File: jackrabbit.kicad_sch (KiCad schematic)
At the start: 62 parts, among them J1 USB_C, J2 PinHeader_2.54mm_02x10, J3 PinHeader_2.54mm_02x04, J4 PinHeader_2.54mm_02x04, J5 PinHeader_2.54mm_01x04, J6 PinHeader_2.54mm_01x03, SW1 SW_Push, SW2 SW_Push, U1 MIC5319-3.3YD5, U2 74LVX245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

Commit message: Continue layout
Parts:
- J2: footprint Connector_PinHeader_2.54mm:PinHeader_2x10_P2.54mm_Horizontal -> jackrabbit:PinHeader_2x10_P2.54mm_Horizontal_NoSilk
- J5: footprint Connector_PinHeader_2.54mm:PinHeader_1x04_P2.54mm_Vertical -> jackrabbit:PinHeader_1x04_P2.54mm_NoSilk
- J6: footprint Connector_PinHeader_2.54mm:PinHeader_1x03_P2.54mm_Vertical -> jackrabbit:PinHeader_1x03_P2.54mm_NoSilk
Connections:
- net ADC0: now also J3.7 (Pin_7)
- net D+: now reaches R4.1, U4.47 (USB_DP)
- net D-: now reaches R5.1, U4.46 (USB_DM)
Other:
- moved on the sheet: R4, R5
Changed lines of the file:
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@@
     (stroke (width 0) (type default) (color 0 0 0 0))
   )
+  (wire (pts (xy 166.37 73.66) (xy 173.99 73.66))
+    (stroke (width 0) (type default) (color 0 0 0 0))
+  )
   (wire (pts (xy 246.38 114.3) (xy 236.22 114.3))
     (stroke (width 0) (type default) (color 0 0 0 0))
@@
     (stroke (width 0) (type default) (color 0 0 0 0))
   )
-  (wire (pts (xy 166.37 73.66) (xy 171.45 73.66))
-    (stroke (width 0) (type default) (color 0 0 0 0))
-  )
   (wire (pts (xy 246.38 68.58) (xy 236.22 68.58))
     (stroke (width 0) (type default) (color 0 0 0 0))
@@
     (stroke (width 0) (type default) (color 0 0 0 0))
   )
-  (wire (pts (xy 176.53 71.12) (xy 186.69 71.12))
+  (wire (pts (xy 179.07 71.12) (xy 189.23 71.12))
     (stroke (width 0) (type default) (color 0 0 0 0))
   )
@@
     (stroke (width 0) (type default) (color 0 0 0 0))
   )
-  (wire (pts (xy 166.37 71.12) (xy 171.45 71.12))
+  (wire (pts (xy 166.37 71.12) (xy 173.99 71.12))
     (stroke (width 0) (type default) (color 0 0 0 0))
   )
@@
     (stroke (width 0) (type default) (color 0 0 0 0))
   )
-  (wire (pts (xy 176.53 73.66) (xy 186.69 73.66))
+  (wire (pts (xy 179.07 73.66) (xy 189.23 73.66))
     (stroke (width 0) (type default) (color 0 0 0 0))
   )
@@
     (effects (font (size 1.27 1.27)) (justify left bottom))
   )
-  (label "USB_D+" (at 186.69 71.12 180)
+  (label "USB_D+" (at 189.23 71.12 180)
     (effects (font (size 1.27 1.27)) (justify right bottom))
   )
@@
     (effects (font (size 1.27 1.27)) (justify right bottom))
   )
+  (label "D-" (at 167.64 73.66 0)
+    (effects (font (size 1.27 1.27)) (justify left bottom))
+  )
+  (label "D+" (at 167.64 71.12 0)
+    (effects (font (size 1.27 1.27)) (justify left bottom))
+  )
   (label "OUT_DIG7" (at 53.34 152.4 180)
     (effects (font (size 1.27 1.27)) (justify right bottom))
@@
     (effects (font (size 1.27 1.27)) (justify right bottom))
   )
-  (label "ADC0" (at 233.68 139.7 0)
+  (label "ADC0" (at 233.68 142.24 0)
     (effects (font (size 1.27 1.27)) (justify left bottom))
   )
@@
     (effects (font (size 1.27 1.27)) (justify left bottom))
   )
-  (label "USB_D-" (at 186.69 73.66 180)
+  (label "USB_D-" (at 189.23 73.66 180)
     (effects (font (size 1.27 1.27)) (justify right bottom))
   )
@@
     (pin "1")
   )
-  (symbol (lib_id "Device:R_Small_US") (at 173.99 71.12 90) (unit 1)
+  (symbol (lib_id "Device:R_Small_US") (at 176.53 71.12 90) (unit 1)
     (in_bom yes) (on_board yes)
-    (property "Reference" "R4" (id 0) (at 170.18 69.85 90))
-    (property "Value" "27" (id 1) (at 176.53 69.85 90))
-    (property "Footprint" "Resistor_SMD:R_0603_1608Metric_Pad0.98x0.95mm_HandSolder" (id 2) (at 173.99 71.12 0)
+    (property "Reference" "R4" (id 0) (at 172.72 69.85 90))
+    (property "Value" "27" (id 1) (at 179.07 69.85 90))
+    (property "Footprint" "Resistor_SMD:R_0603_1608Metric_Pad0.98x0.95mm_HandSolder" (id 2) (at 176.53 71.12 0)
       (effects (font (size 1.27 1.27)) hide)
     )
-    (property "Datasheet" "~" (id 3) (at 173.99 71.12 0)
+    (property "Datasheet" "~" (id 3) (at 176.53 71.12 0)
       (effects (font (size 1.27 1.27)) hide)
     )
@@
     (property "Reference" "J2" (id 0) (at 36.83 139.7 0))
     (property "Value" "PinHeader_2.54mm_02x10" (id 1) (at 36.83 167.64 0))
-    (property "Footprint" "Connector_PinHeader_2.54mm:PinHeader_2x10_P2.54mm_Horizontal" (id 2) (at 35.56 154.94 0)
+    (property "Footprint" "jackrabbit:PinHeader_2x10_P2.54mm_Horizontal_NoSilk" (id 2) (at 35.56 154.94 0)
       (effects (font (size 1.27 1.27)) hide)
     )
@@
     (pin "1")
   )
-  (symbol (lib_id "Device:R_Small_US") (at 173.99 73.66 90) (unit 1)
+  (symbol (lib_id "Device:R_Small_US") (at 176.53 73.66 90) (unit 1)
     (in_bom yes) (on_board yes)
-    (property "Reference" "R5" (id 0) (at 170.18 72.39 90))
-    (property "Value" "27" (id 1) (at 176.53 72.39 90))
-    (property "Footprint" "Resistor_SMD:R_0603_1608Metric_Pad0.98x0.95mm_HandSolder" (id 2) (at 173.99 73.66 0)
+    (property "Reference" "R5" (id 0) (at 172.72 72.39 90))
+    (property "Value" "27" (id 1) (at 179.07 72.39 90))
+    (property "Footprint" "Resistor_SMD:R_0603_1608Metric_Pad0.98x0.95mm_HandSolder" (id 2) (at 176.53 73.66 0)
       (effects (font (size 1.27 1.27)) hide)
     )
-    (property "Datasheet" "~" (id 3) (at 173.99 73.66 0)
+    (property "Datasheet" "~" (id 3) (at 176.53 73.66 0)
       (effects (font (size 1.27 1.27)) hide)
     )
@@
     (property "Reference" "J6" (id 0) (at 30.48 186.69 0))
     (property "Value" "PinHeader_2.54mm_01x03" (id 1) (at 30.48 196.85 0))
-    (property "Footprint" "Connector_PinHeader_2.54mm:PinHeader_1x03_P2.54mm_Vertical" (id 2) (at 30.48 191.77 0)
+    (property "Footprint" "jackrabbit:PinHeader_1x03_P2.54mm_NoSilk" (id 2) (at 30.48 191.77 0)
       (effects (font (size 1.27 1.27)) hide)
     )
@@
     (property "Reference" "J5" (id 0) (at 200.66 152.4 0))
     (property "Value" "PinHeader_2.54mm_01x04" (id 1) (at 200.66 165.1 0))
-    (property "Footprint" "Connector_PinHeader_2.54mm:PinHeader_1x04_P2.54mm_Vertical" (id 2) (at 200.66 157.48 0)
+    (property "Footprint" "jackrabbit:PinHeader_1x04_P2.54mm_NoSilk" (id 2) (at 200.66 157.48 0)
       (effects (font (size 1.27 1.27)) hide)
     )
@@
     )
     (path "/791214ba-3f08-4a8f-b2f1-03e7cde5a47c"
-      (reference "J2") (unit 1) (value "PinHeader_2.54mm_02x10") (footprint "Connector_PinHeader_2.54mm:PinHeader_2x10_P2.54mm_Horizontal")
+      (reference "J2") (unit 1) (value "PinHeader_2.54mm_02x10") (footprint "jackrabbit:PinHeader_2x10_P2.54mm_Horizontal_NoSilk")
     )
     (path "/41267881-d459-44ec-a16d-7e8810cd8184"
@@
     )
     (path "/c422dfdf-189d-45aa-8572-20905ff07ea7"
-      (reference "J5") (unit 1) (value "PinHeader_2.54mm_01x04") (footprint "Connector_PinHeader_2.54mm:PinHeader_1x04_P2.54mm_Vertical")
+      (reference "J5") (unit 1) (value "PinHeader_2.54mm_01x04") (footprint "jackrabbit:PinHeader_1x04_P2.54mm_NoSilk")
     )
     (path "/bbb69503-a53a-4fa5-9940-c051d2dd833e"
-      (reference "J6") (unit 1) (value "PinHeader_2.54mm_01x03") (footprint "Connector_PinHeader_2.54mm:PinHeader_1x03_P2.54mm_Vertical")
+      (reference "J6") (unit 1) (value "PinHeader_2.54mm_01x03") (footprint "jackrabbit:PinHeader_1x03_P2.54mm_NoSilk")
     )
     (path "/92912fe5-8afd-4b87-83be-55234c82a217"

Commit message: Continue layout
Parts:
- J3, J4: footprint Connector_PinHeader_2.54mm:PinHeader_2x04_P2.54mm_Horizontal -> jackrabbit:PinHeader_2x04_P2.54mm_NoSilk
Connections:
- net ~{DIR_OUT_B}: now also U4.29 (GPIO18); no longer U4.28 (GPIO17)
- net ~{OE_A}: now also U4.28 (GPIO17); no longer U4.31 (GPIO20)
- net ~{OE_B}: now also U4.30 (GPIO19); no longer U4.32 (GPIO21)
- net at R7.1: now also U4.31 (GPIO20); no longer U4.29 (GPIO18)
- net at R8.1: now also U4.32 (GPIO21); no longer U4.30 (GPIO19)
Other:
- moved on the sheet: R7, R8
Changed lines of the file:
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@@
     (stroke (width 0) (type default) (color 0 0 0 0))
   )
-  (wire (pts (xy 176.53 127) (xy 187.96 127))
+  (wire (pts (xy 176.53 132.08) (xy 187.96 132.08))
     (stroke (width 0) (type default) (color 0 0 0 0))
   )
@@
     (stroke (width 0) (type default) (color 0 0 0 0))
   )
-  (wire (pts (xy 176.53 129.54) (xy 187.96 129.54))
+  (wire (pts (xy 176.53 134.62) (xy 187.96 134.62))
     (stroke (width 0) (type default) (color 0 0 0 0))
   )
@@
     (stroke (width 0) (type default) (color 0 0 0 0))
   )
-  (wire (pts (xy 166.37 132.08) (xy 177.8 132.08))
+  (wire (pts (xy 166.37 124.46) (xy 177.8 124.46))
     (stroke (width 0) (type default) (color 0 0 0 0))
   )
@@
     (stroke (width 0) (type default) (color 0 0 0 0))
   )
-  (wire (pts (xy 166.37 134.62) (xy 177.8 134.62))
+  (wire (pts (xy 166.37 129.54) (xy 177.8 129.54))
     (stroke (width 0) (type default) (color 0 0 0 0))
   )
@@
     (stroke (width 0) (type default) (color 0 0 0 0))
   )
-  (wire (pts (xy 166.37 129.54) (xy 171.45 129.54))
+  (wire (pts (xy 166.37 134.62) (xy 171.45 134.62))
     (stroke (width 0) (type default) (color 0 0 0 0))
   )
@@
     (stroke (width 0) (type default) (color 0 0 0 0))
   )
-  (wire (pts (xy 166.37 124.46) (xy 177.8 124.46))
+  (wire (pts (xy 166.37 127) (xy 177.8 127))
     (stroke (width 0) (type default) (color 0 0 0 0))
   )
@@
     (stroke (width 0) (type default) (color 0 0 0 0))
   )
-  (wire (pts (xy 166.37 127) (xy 171.45 127))
+  (wire (pts (xy 166.37 132.08) (xy 171.45 132.08))
     (stroke (width 0) (type default) (color 0 0 0 0))
   )
@@
     (effects (font (size 1.27 1.27)) (justify right bottom))
   )
-  (label "RX" (at 187.96 129.54 180)
+  (label "RX" (at 187.96 134.62 180)
     (effects (font (size 1.27 1.27)) (justify right bottom))
   )
@@
     (effects (font (size 1.27 1.27)) (justify left bottom))
   )
-  (label "~{OE_B}" (at 177.8 134.62 180)
+  (label "~{OE_B}" (at 177.8 129.54 180)
     (effects (font (size 1.27 1.27)) (justify right bottom))
   )
@@
     (effects (font (size 1.27 1.27)) (justify left bottom))
   )
-  (label "TX" (at 187.96 127 180)
+  (label "TX" (at 187.96 132.08 180)
     (effects (font (size 1.27 1.27)) (justify right bottom))
   )
@@
     (effects (font (size 1.27 1.27)) (justify right bottom))
   )
-  (label "~{DIR_OUT_B}" (at 177.8 124.46 180)
+  (label "~{DIR_OUT_B}" (at 177.8 127 180)
     (effects (font (size 1.27 1.27)) (justify right bottom))
   )
@@
     (effects (font (size 1.27 1.27)) (justify left bottom))
   )
-  (label "~{OE_A}" (at 177.8 132.08 180)
+  (label "~{OE_A}" (at 177.8 124.46 180)
     (effects (font (size 1.27 1.27)) (justify right bottom))
   )
@@
     (property "Reference" "J3" (id 0) (at 250.19 139.7 0))
     (property "Value" "PinHeader_2.54mm_02x04" (id 1) (at 250.19 152.4 0))
-    (property "Footprint" "Connector_PinHeader_2.54mm:PinHeader_2x04_P2.54mm_Horizontal" (id 2) (at 248.92 147.32 0)
+    (property "Footprint" "jackrabbit:PinHeader_2x04_P2.54mm_NoSilk" (id 2) (at 248.92 147.32 0)
       (effects (font (size 1.27 1.27)) hide)
     )
@@
     (property "Reference" "J4" (id 0) (at 250.19 154.94 0))
     (property "Value" "PinHeader_2.54mm_02x04" (id 1) (at 250.19 167.64 0))
-    (property "Footprint" "Connector_PinHeader_2.54mm:PinHeader_2x04_P2.54mm_Horizontal" (id 2) (at 248.92 160.02 0)
+    (property "Footprint" "jackrabbit:PinHeader_2x04_P2.54mm_NoSilk" (id 2) (at 248.92 160.02 0)
       (effects (font (size 1.27 1.27)) hide)
     )
@@
     (pin "1")
   )
-  (symbol (lib_id "Device:R_Small_US") (at 173.99 129.54 90) (unit 1)
+  (symbol (lib_id "Device:R_Small_US") (at 173.99 134.62 90) (unit 1)
     (in_bom yes) (on_board yes)
-    (property "Reference" "R8" (id 0) (at 170.18 128.27 90))
-    (property "Value" "100" (id 1) (at 177.8 128.27 90))
-    (property "Footprint" "Resistor_SMD:R_0603_1608Metric_Pad0.98x0.95mm_HandSolder" (id 2) (at 173.99 129.54 0)
+    (property "Reference" "R8" (id 0) (at 170.18 133.35 90))
+    (property "Value" "100" (id 1) (at 177.8 133.35 90))
+    (property "Footprint" "Resistor_SMD:R_0603_1608Metric_Pad0.98x0.95mm_HandSolder" (id 2) (at 173.99 134.62 0)
       (effects (font (size 1.27 1.27)) hide)
     )
-    (property "Datasheet" "~" (id 3) (at 173.99 129.54 0)
+    (property "Datasheet" "~" (id 3) (at 173.99 134.62 0)
       (effects (font (size 1.27 1.27)) hide)
     )
@@
     (pin "2")
   )
-  (symbol (lib_id "Device:R_Small_US") (at 173.99 127 90) (unit 1)
+  (symbol (lib_id "Device:R_Small_US") (at 173.99 132.08 90) (unit 1)
     (in_bom yes) (on_board yes)
-    (property "Reference" "R7" (id 0) (at 170.18 125.73 90))
-    (property "Value" "100" (id 1) (at 177.8 125.73 90))
-    (property "Footprint" "Resistor_SMD:R_0603_1608Metric_Pad0.98x0.95mm_HandSolder" (id 2) (at 173.99 127 0)
+    (property "Reference" "R7" (id 0) (at 170.18 130.81 90))
+    (property "Value" "100" (id 1) (at 177.8 130.81 90))
+    (property "Footprint" "Resistor_SMD:R_0603_1608Metric_Pad0.98x0.95mm_HandSolder" (id 2) (at 173.99 132.08 0)
       (effects (font (size 1.27 1.27)) hide)
     )
-    (property "Datasheet" "~" (id 3) (at 173.99 127 0)
+    (property "Datasheet" "~" (id 3) (at 173.99 132.08 0)
       (effects (font (size 1.27 1.27)) hide)
     )
@@
     )
     (path "/41267881-d459-44ec-a16d-7e8810cd8184"
-      (reference "J3") (unit 1) (value "PinHeader_2.54mm_02x04") (footprint "Connector_PinHeader_2.54mm:PinHeader_2x04_P2.54mm_Horizontal")
+      (reference "J3") (unit 1) (value "PinHeader_2.54mm_02x04") (footprint "jackrabbit:PinHeader_2x04_P2.54mm_NoSilk")
     )
     (path "/42c076d8-84e3-453f-aa5b-cae6866038f5"
-      (reference "J4") (unit 1) (value "PinHeader_2.54mm_02x04") (footprint "Connector_PinHeader_2.54mm:PinHeader_2x04_P2.54mm_Horizontal")
+      (reference "J4") (unit 1) (value "PinHeader_2.54mm_02x04") (footprint "jackrabbit:PinHeader_2x04_P2.54mm_NoSilk")
     )
     (path "/c422dfdf-189d-45aa-8572-20905ff07ea7"

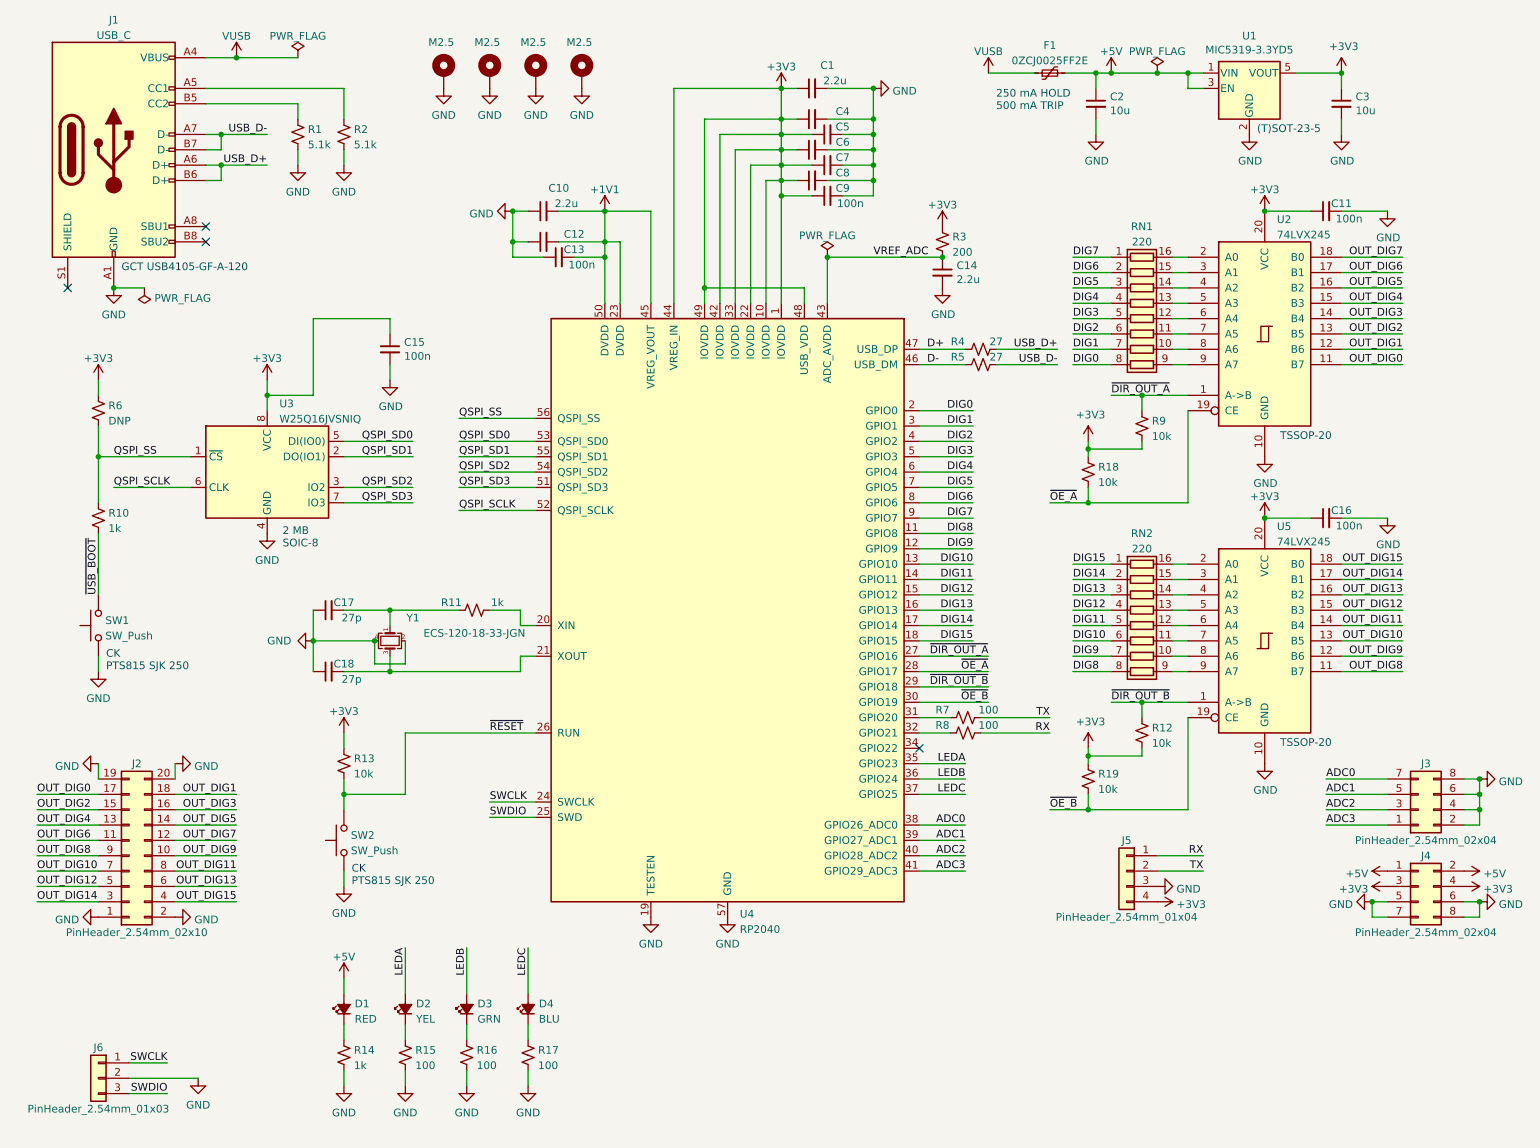
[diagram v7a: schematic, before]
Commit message: Continue layout; add labels for digital connector
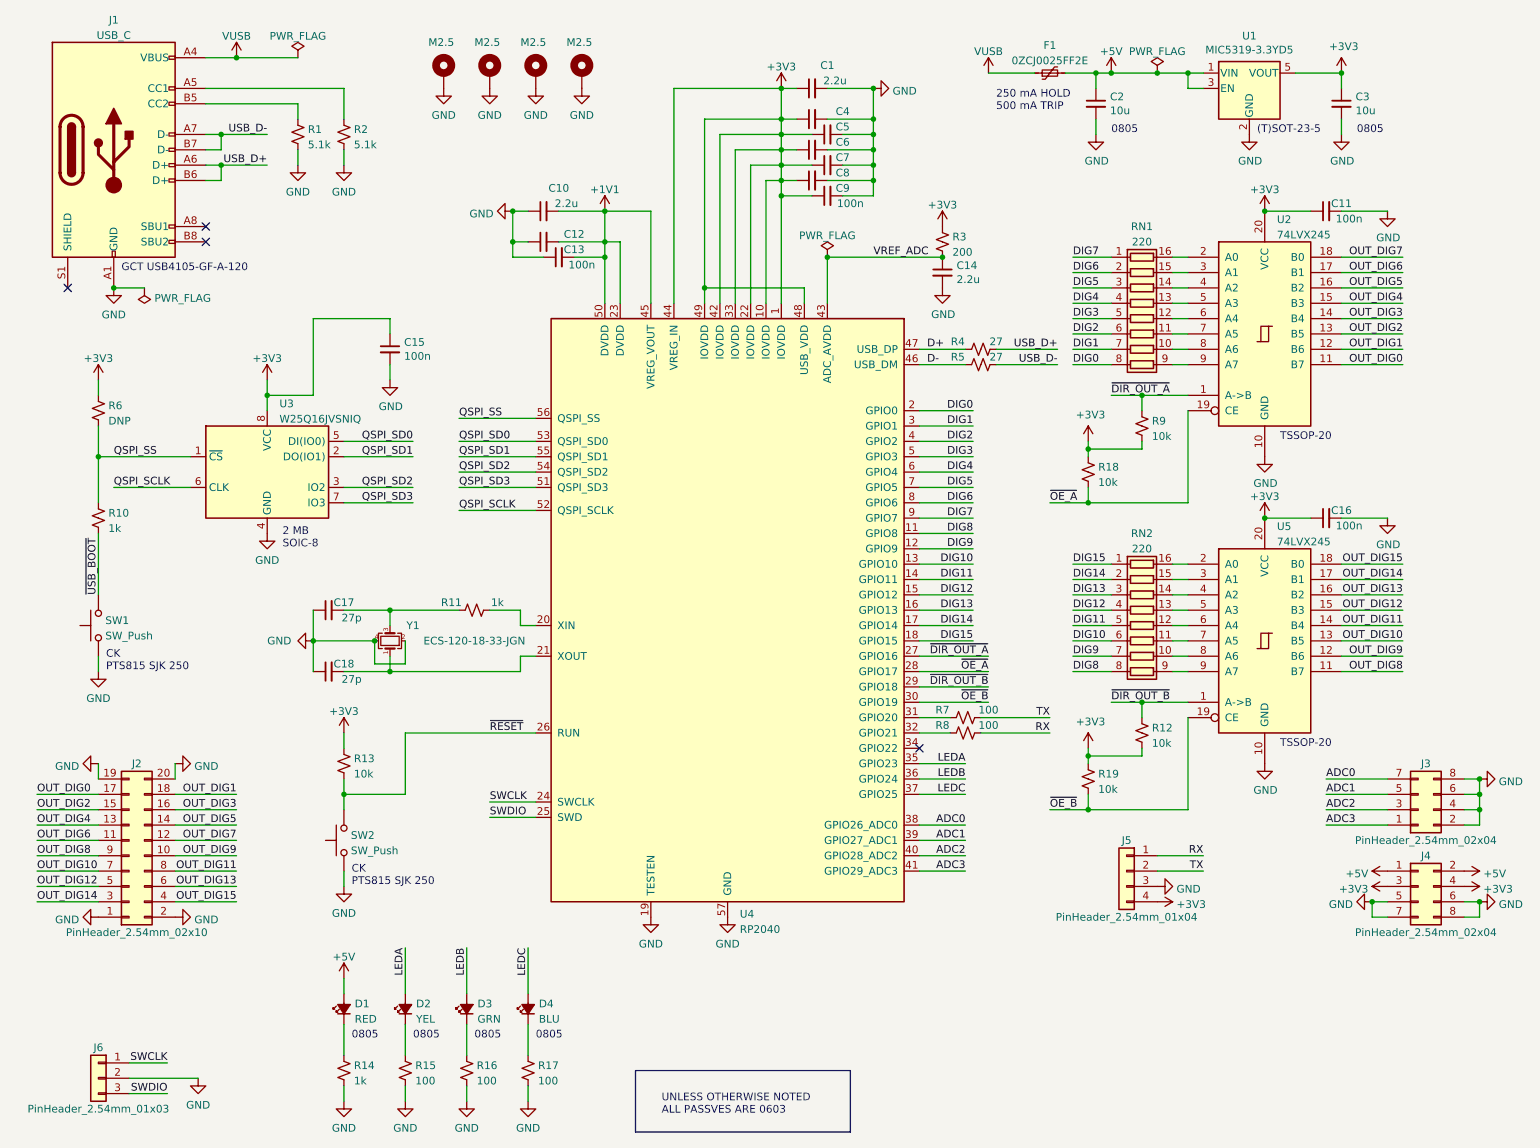
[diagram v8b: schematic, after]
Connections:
- net at C17.2, R11.1: now also Y1.3; no longer Y1.1
- net at C18.2, U4.21 (XOUT): now also Y1.1; no longer Y1.3
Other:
- note added: "0805"
- note added: "UNLESS OTHERWISE NOTED ALL PASSVES ARE 0603"
- moved on the sheet: R14, R15, R16, R17
